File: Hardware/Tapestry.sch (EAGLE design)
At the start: 81 parts, among them U1 ATSAMS70NXXA-AN, U2 AK4618VQ, U3 V_REG_MIC2920, U4 V_REG_MIC2920, Y1 12MHz

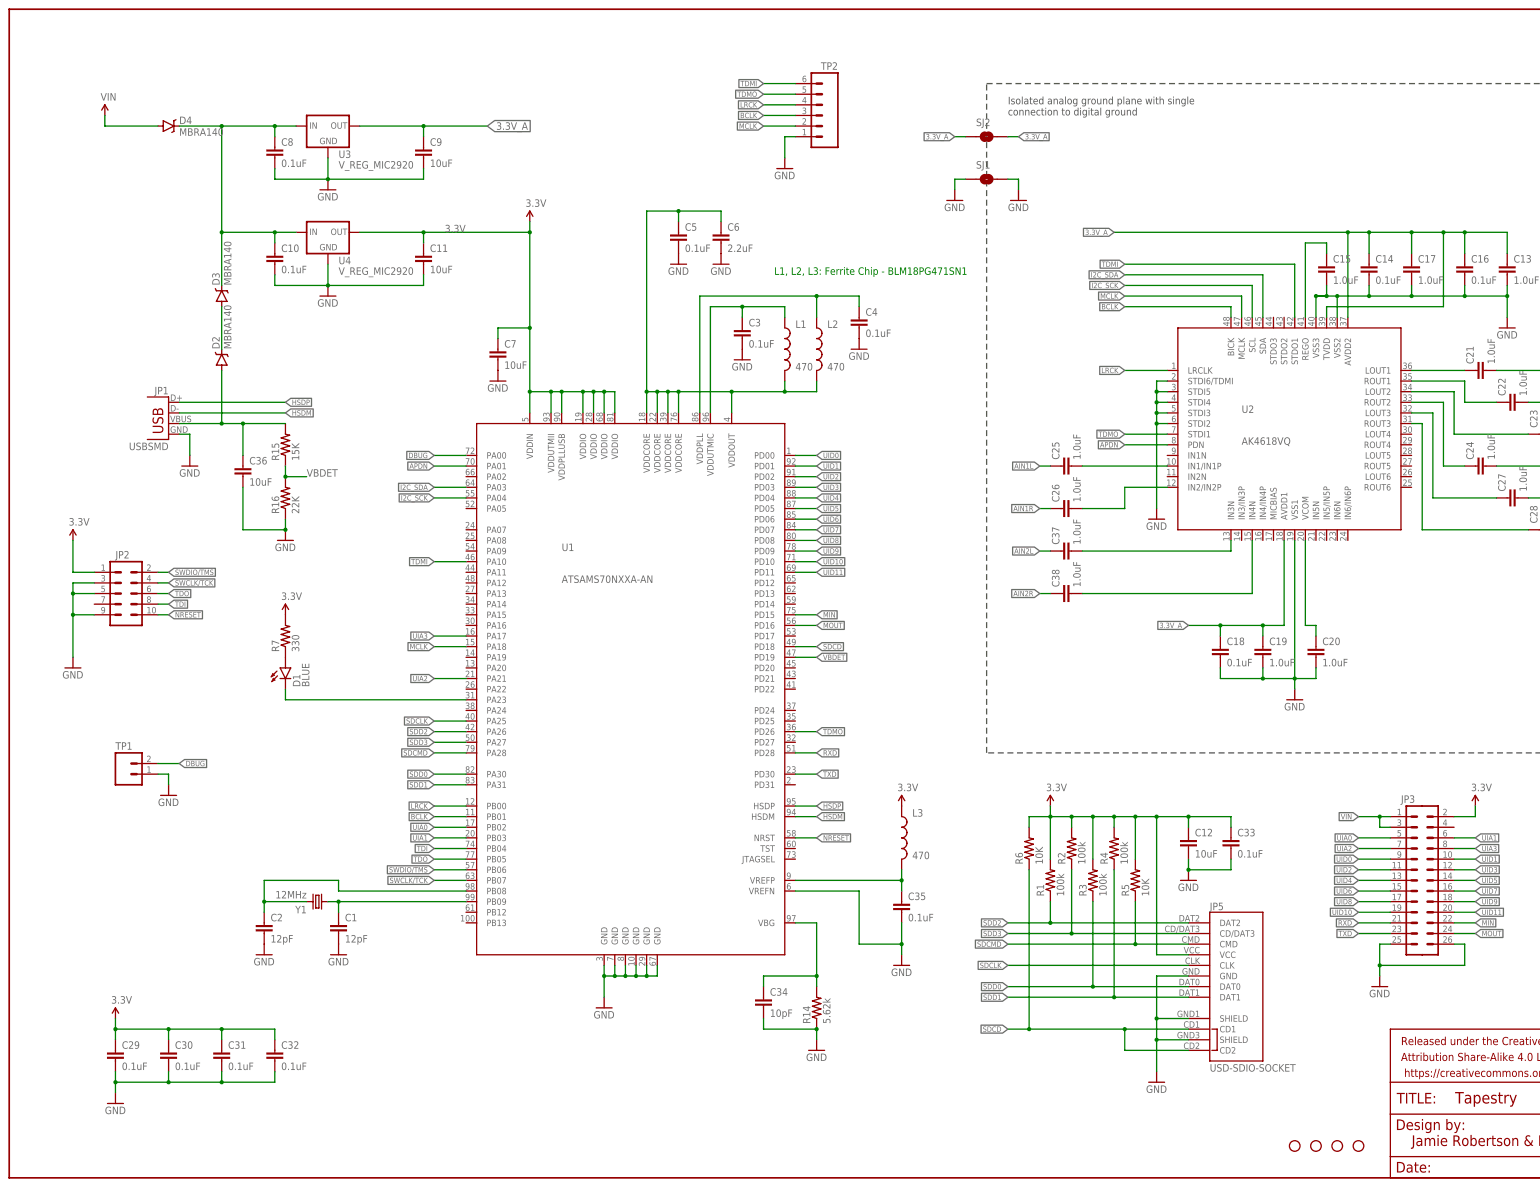
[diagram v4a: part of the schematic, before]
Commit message: Ongoing progress.
Filled out "layout checklist" in Atmel docs.
Pushed & pulled components to closer to final proximity.
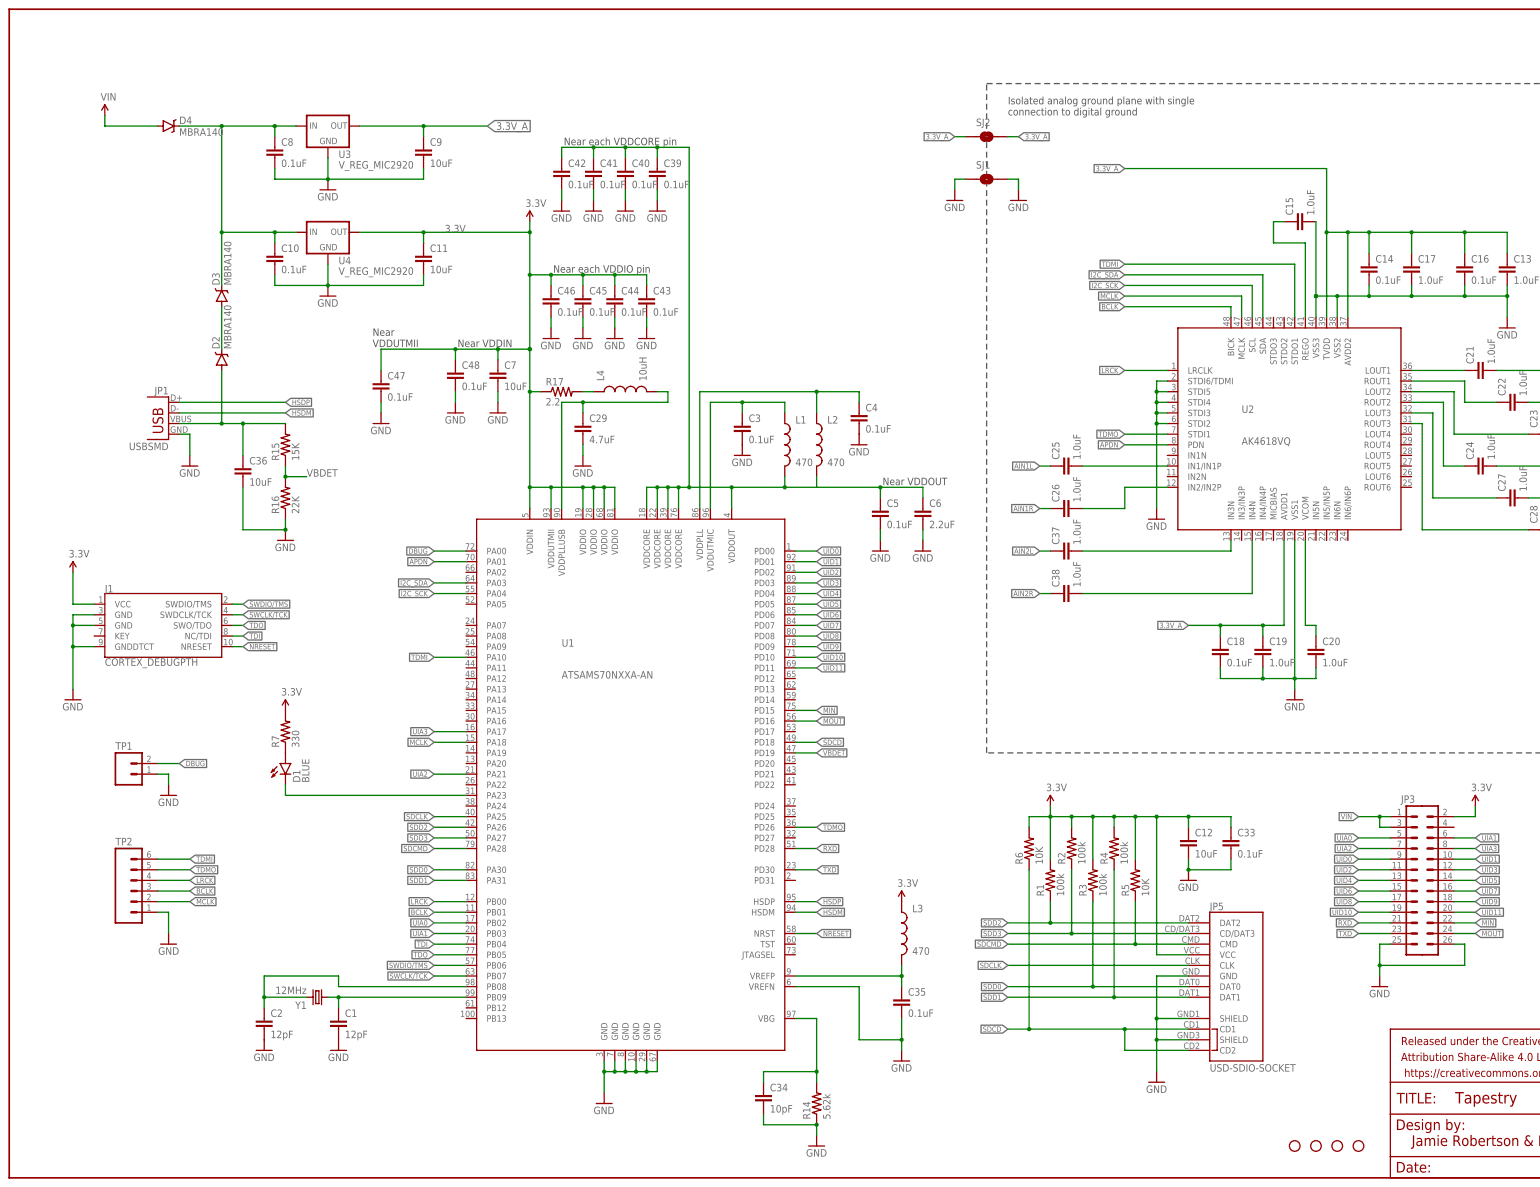
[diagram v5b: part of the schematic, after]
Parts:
- removed C30, C31, C32: 0.1uF, SparkFun-Capacitors:0.1UF-100V-10%(0603)
- removed JP2: (no value), SparkFun-Connectors:M05X20.05_IN_PTH_SILK
- added C39, C40, C41, C42, C43, C44, C45, C46, C47, C48: 0.1uF, SparkFun-Capacitors:0.1UF-25V(+80/-20%)(0603)
- added J1: CORTEX_DEBUGPTH, SparkFun-Connectors:CORTEX_DEBUGPTH
- added L4: 10uH, SparkFun-Passives:INDUCTOR0805
- added R17: 2.2, SparkFun-Resistors:2.2OHM-1/10W-5%(0603)
- C29: value 0.1uF -> 4.7uF; device SparkFun-Capacitors:0.1UF-100V-10%(0603) -> SparkFun-Capacitors:4.7UF-6.3V-10%(0603)0603
- L1, L2, L3: PROD_ID (none) -> NDUC-12579
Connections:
- new net N$24: L4.1, R17.2
- new net VDDOUT: C39.1, C40.1, C41.1, C42.1, C5.1, C6.1, L1.2, L2.2, U1.VDDCORE@1, U1.VDDCORE@2, U1.VDDCORE@3, U1.VDDCORE@4, U1.VDDOUT
- net 3.3V: now also C43.1, C44.1, C45.1, C46.1, C47.1, C48.1, J1.VCC, R17.1; no longer C29.1, C30.1, C31.1, C32.1, JP2.1, U1.VDDPLLUSB
- net GND: now also C39.2, C40.2, C41.2, C42.2, C43.2, C44.2, C45.2, C46.2, C47.2, C48.2, J1.GND@3, J1.GND@5, J1.GNDDTCT; no longer C30.2, C31.2, C32.2, JP2.3, JP2.5, JP2.9
- net N$4: now also C29.1, L4.2, U1.VDDPLLUSB; no longer C5.1, C6.1, L1.2, L2.2, U1.VDDCORE@1, U1.VDDCORE@2, U1.VDDCORE@3, U1.VDDCORE@4, U1.VDDOUT
- net NRESET: now also J1.NRESET; no longer JP2.10
- net SWCLK/TCK: now also J1.SWDCLK/TCK; no longer JP2.4
- net SWDIO/TMS: now also J1.SWDIO/TMS; no longer JP2.2
- net TDI: now also J1.NC/TDI; no longer JP2.8
- net TDO: now also J1.SWO/TDO; no longer JP2.6
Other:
- note added: "Near VDDIN"
- note added: "Near VDDOUT"
- note added: "Near VDDUTMII"
- note added: "Near each VDDCORE pin"
- note added: "Near each VDDIO pin"
- note removed: "L1, L2, L3: Ferrite Chip - BLM18PG471SN1"
- moved on the sheet: C1, C15, C2, C29, C3, C34, C35, C4, C5, C6, C7, D1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

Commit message: Updates all around
Adjusted LQFP land patterns.
Switched to LM1117 Vregs.
Added library to gitignore.
Ongoing ratsnest work.
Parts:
- added R18, R19: 240, SparkFun-Resistors:240OHM1/10W1%(0603)
- added R20, R21: 390, SparkFun-Resistors:390OHM1/10W1%(0603)
- SJ1, SJ2: value SOLDERJUMPERTRACE -> JUMPER-PAD-2-NC_BY_TRACE; device SparkFun-Retired:SOLDERJUMPERTRACE -> SparkFun-Passives:JUMPER-PAD-2-NC_BY_TRACE
- U2: value AK4618VQ -> AK4618VQSFE-PACKAGE; device tapestry:AK4618VQ -> tapestry:AK4618VQSFE-PACKAGE
- U3, U4: value V_REG_MIC2920 -> (none); device SparkFun-PowerIC:V_REG_MIC2920 -> SparkFun-PowerIC:V_REG_LM1117SOT223
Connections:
- new net N$25: R18.1, R20.2, U3.ADJ
- new net N$29: R19.1, R21.2, U4.ADJ
- net 3.3V: now also JP3.4, R19.2, U4.OUT@1
- net 3.3V_A: now also R18.2, U3.OUT@1
- net AIN1L: now also JP4.13; no longer JP4.1
- net AIN1R: now also JP4.15; no longer JP4.3
- net AIN2L: now also JP4.17; no longer JP4.5
- net AIN2R: now also JP4.19; no longer JP4.7
- net AOUT1L: now also JP4.1; no longer JP4.9
- net AOUT1R: now also JP4.3; no longer JP4.11
- net AOUT2L: now also JP4.5; no longer JP4.13
- net AOUT2R: now also JP4.7; no longer JP4.15
- net AOUT3L: now also JP4.9; no longer JP4.17
- net AOUT3R: now also JP4.11; no longer JP4.19
- net GND: now also R20.1, R21.1; no longer U3.GND, U4.GND
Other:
- moved on the sheet: C10, C11, C39, C40, C41, C42, C8, C9, D3, D4

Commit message: More updates.
Schematic logos, partitioning & labeling.
Found a few more absent pullup resistors.
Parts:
- added LOGO1: SFE_LOGO_NAME_FLAME.2_INCH, SparkFun-Aesthetics:SFE_LOGO_NAME_FLAME.2_INCH
- added R22, R23, R24: 100k, SparkFun-Resistors:100KOHM-1/10W-1%(0603)
- added R25, R26: 4.7K, SparkFun-Resistors:4.7KOHM-1/10W-1%(0603)
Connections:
- net 3.3V: now also R22.2, R23.2, R24.2, R25.2, R26.2
- net I2C_SCK: now also R26.1
- net I2C_SDA: now also R25.1
- net NRESET: now also R24.1
- net SWCLK/TCK: now also R23.1
- net SWDIO/TMS: now also R22.1
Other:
- note added: "??"
- note added: "Audio Codec"
- note added: "Cortex Debug Port"
- note added: "Cortex M7 Processor"
- note added: "I2S Test Points"
- note added: "Power Regulators"
- note added: "SDIO uSD Card Slot"
- note added: "USB Device Port"
- note added: "User Input Pins"
- moved on the sheet: C1, C10, C11, C12, C2, C29, C3, C33, C34, C35, C36, C39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

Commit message: WIP.
Checking in so I can traverse project history for a moment.
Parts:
- added J2: POWER_JACKPTH_LOCK, SparkFun-Connectors:POWER_JACKPTH_LOCK
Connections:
- net GND: now also J2.GND, J2.GNDBREAK
- net VIN: now also J2.PWR
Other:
- moved on the sheet: D4
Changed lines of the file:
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@@
 <part name="R26" library="SparkFun-Resistors" deviceset="4.7KOHM-1/10W-1%(0603)" device="" value="4.7K"/>
 <part name="LOGO1" library="SparkFun-Aesthetics" deviceset="SFE_LOGO_NAME_FLAME" device=".2_INCH"/>
+<part name="J2" library="SparkFun-Connectors" deviceset="POWER_JACK" device="PTH_LOCK"/>
+<part name="GND43" library="SparkFun-Aesthetics" deviceset="GND" device=""/>
 </parts>
 <sheets>
@@
 <text x="109.22" y="271.78" size="3.81" layer="97">Cortex M7 Processor</text>
 <text x="238.76" y="264.16" size="3.81" layer="97">Audio Codec</text>
-<text x="236.22" y="93.98" size="3.81" layer="97">SDIO uSD Card Slot</text>
-<text x="332.74" y="93.98" size="3.81" layer="97">User Input Pins</text>
+<text x="236.22" y="96.52" size="3.81" layer="97">SDIO uSD Card Slot</text>
+<text x="332.74" y="96.52" size="3.81" layer="97">User Input Pins</text>
 </plain>
 <instances>
@@
 <instance part="D2" gate="G$1" x="38.1" y="193.04" rot="R90"/>
 <instance part="D3" gate="G$1" x="38.1" y="205.74" rot="R90"/>
-<instance part="D4" gate="G$1" x="25.4" y="256.54"/>
+<instance part="D4" gate="G$1" x="30.48" y="256.54"/>
 <instance part="U3" gate="G$1" x="58.42" y="261.62"/>
 <instance part="U4" gate="G$1" x="58.42" y="220.98"/>
@@
 <instance part="GND17" gate="1" x="30.48" y="63.5" rot="MR0"/>
 <instance part="TP2" gate="G$1" x="22.86" y="76.2"/>
-<instance part="SUPPLY6" gate="G$1" x="10.16" y="259.08"/>
+<instance part="SUPPLY6" gate="G$1" x="22.86" y="264.16"/>
 <instance part="C21" gate="G$1" x="353.06" y="193.04" rot="R90"/>
 <instance part="C22" gate="G$1" x="360.68" y="185.42" rot="R90"/>
@@
 <instance part="R26" gate="G$1" x="104.14" y="149.86" rot="R90"/>
 <instance part="LOGO1" gate="G$1" x="271.78" y="0"/>
+<instance part="J2" gate="G$1" x="15.24" y="248.92"/>
+<instance part="GND43" gate="1" x="20.32" y="243.84"/>
 </instances>
 <busses>
@@
 <pinref part="R21" gate="G$1" pin="1"/>
 <wire x1="58.42" y1="193.04" x2="58.42" y2="190.5" width="0.1524" layer="91"/>
+</segment>
+<segment>
+<pinref part="GND43" gate="1" pin="GND"/>
+<wire x1="20.32" y1="246.38" x2="20.32" y2="251.46" width="0.1524" layer="91"/>
+<pinref part="J2" gate="G$1" pin="GNDBREAK"/>
+<wire x1="20.32" y1="251.46" x2="20.32" y2="254" width="0.1524" layer="91"/>
+<wire x1="20.32" y1="254" x2="17.78" y2="254" width="0.1524" layer="91"/>
+<pinref part="J2" gate="G$1" pin="GND"/>
+<wire x1="17.78" y1="251.46" x2="20.32" y2="251.46" width="0.1524" layer="91"/>
+<junction x="20.32" y="251.46"/>
 </segment>
 </net>
@@
 <pinref part="D4" gate="G$1" pin="C"/>
 <wire x1="45.72" y1="261.62" x2="50.8" y2="261.62" width="0.1524" layer="91"/>
-<wire x1="27.94" y1="256.54" x2="38.1" y2="256.54" width="0.1524" layer="91"/>
+<wire x1="33.02" y1="256.54" x2="38.1" y2="256.54" width="0.1524" layer="91"/>
 <pinref part="U4" gate="G$1" pin="IN"/>
 <wire x1="38.1" y1="220.98" x2="45.72" y2="220.98" width="0.1524" layer="91"/>
@@
 <segment>
 <pinref part="D4" gate="G$1" pin="A"/>
-<wire x1="10.16" y1="256.54" x2="22.86" y2="256.54" width="0.1524" layer="91"/>
+<wire x1="22.86" y1="256.54" x2="27.94" y2="256.54" width="0.1524" layer="91"/>
 <pinref part="SUPPLY6" gate="G$1" pin="VIN"/>
-<wire x1="10.16" y1="259.08" x2="10.16" y2="256.54" width="0.1524" layer="91"/>
-</segment>
-<segment>
+<wire x1="22.86" y1="264.16" x2="22.86" y2="256.54" width="0.1524" layer="91"/>
+<pinref part="J2" gate="G$1" pin="PWR"/>
+<wire x1="17.78" y1="256.54" x2="22.86" y2="256.54" width="0.1524" layer="91"/>
+<junction x="22.86" y="256.54"/>
+</segment>
+<segment>
